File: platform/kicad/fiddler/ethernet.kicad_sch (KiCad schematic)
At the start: 33 parts, among them T1 PT61018PEL, U3 LAN8720A

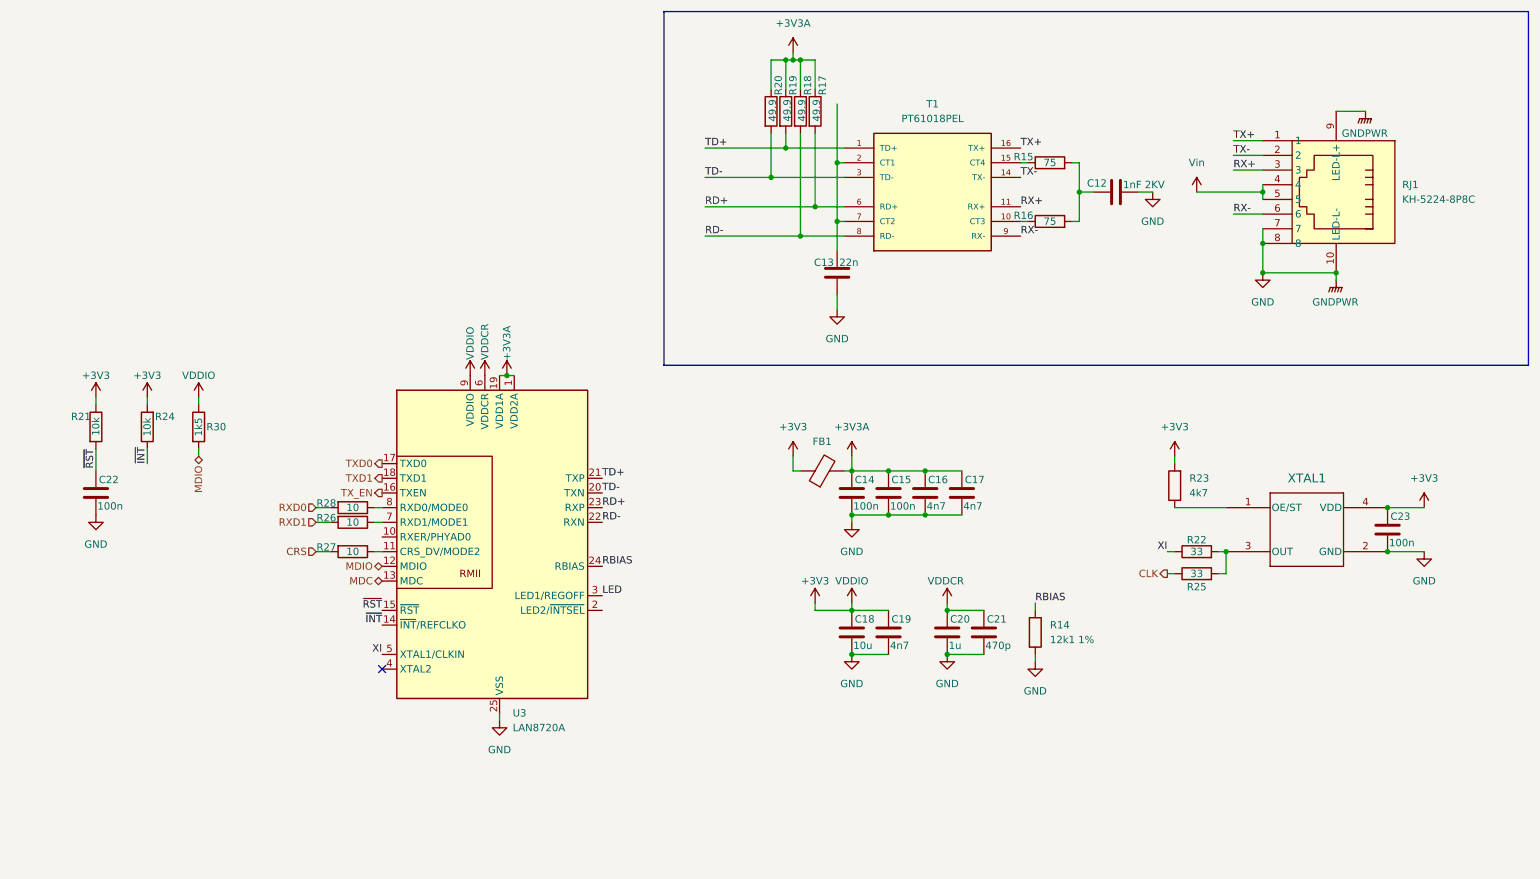
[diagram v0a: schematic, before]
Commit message: Fiddler Ray Speaker: Complete first revision
This change completes the first iteration schematic and layout for the fiddler ray speaker PCB.
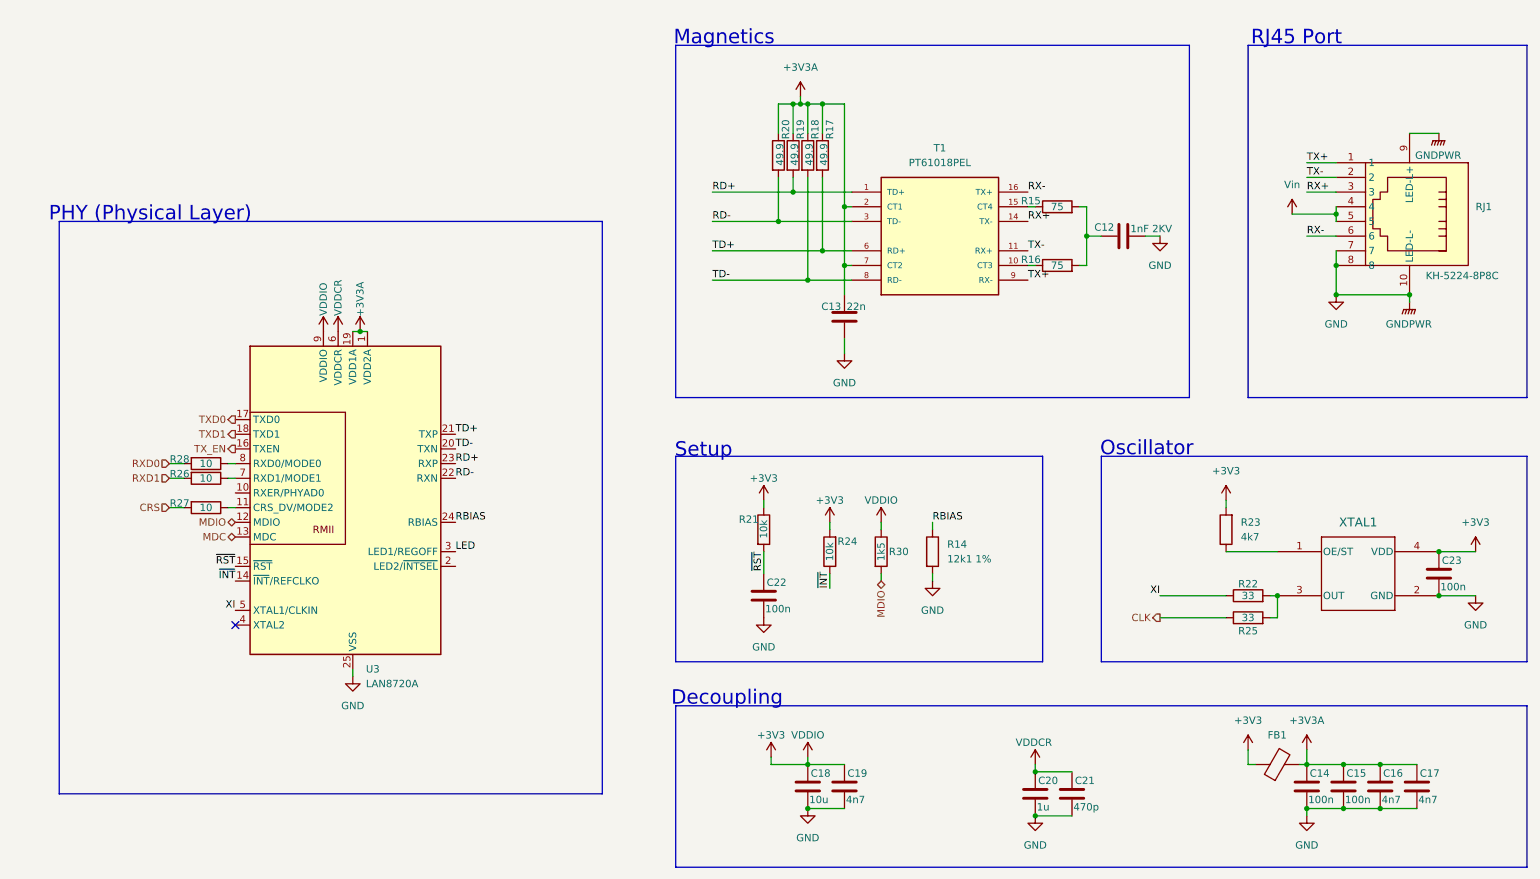
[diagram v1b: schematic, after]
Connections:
- net +3V3A: now also C13.2, T1.2 (CT1), T1.7 (CT2)
- net RD+: now also R19.2, T1.1 (TD+); no longer R17.2, T1.6 (RD+)
- net RD-: now also R20.2, T1.3 (TD-); no longer R18.2, T1.8 (RD-)
- net RX+: now also T1.14 (TX-); no longer T1.11 (RX+)
- net RX-: now also T1.16 (TX+); no longer T1.9 (RX-)
- net TD+: now also R17.2, T1.6 (RD+); no longer R19.2, T1.1 (TD+)
- net TD-: now also R18.2, T1.8 (RD-); no longer R20.2, T1.3 (TD-)
- net TX+: now also T1.9 (RX-); no longer T1.16 (TX+)
- net TX-: now also T1.11 (RX+); no longer T1.14 (TX-)
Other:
- note added: "Decoupling"
- note added: "Magnetics"
- note added: "Oscillator"
- note added: "PHY (Physical Layer)"
- note added: "RJ45 Port"
- note added: "Setup"
- company: (none) -> The Australian Ocean Laboratory
- title: (none) -> Fiddler Ray Speaker Unit V1
- moved on the sheet: C12, C13, C14, C15, C16, C17, C18, C19, C20, C21, C22, C23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

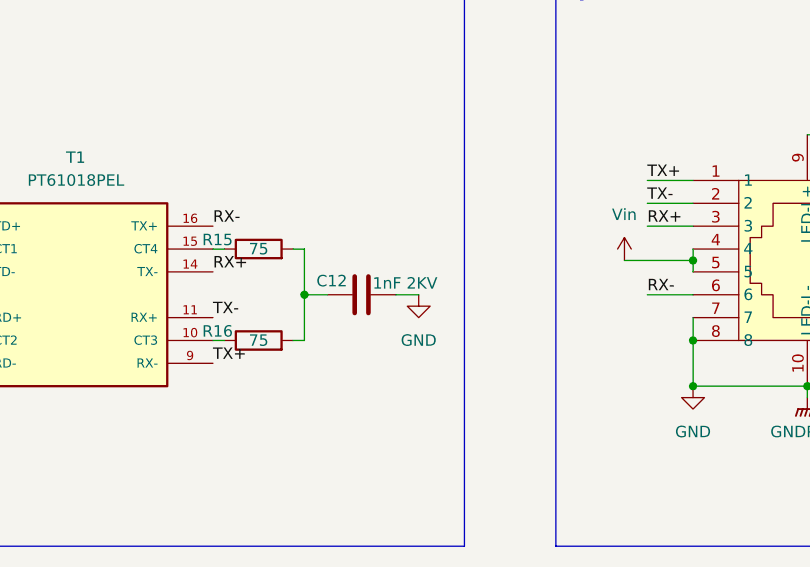
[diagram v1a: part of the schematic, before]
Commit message: Fiddler Ray Speaker: Production rev A
This change adds additional data to components to populate SPN for
the BOM via JLC
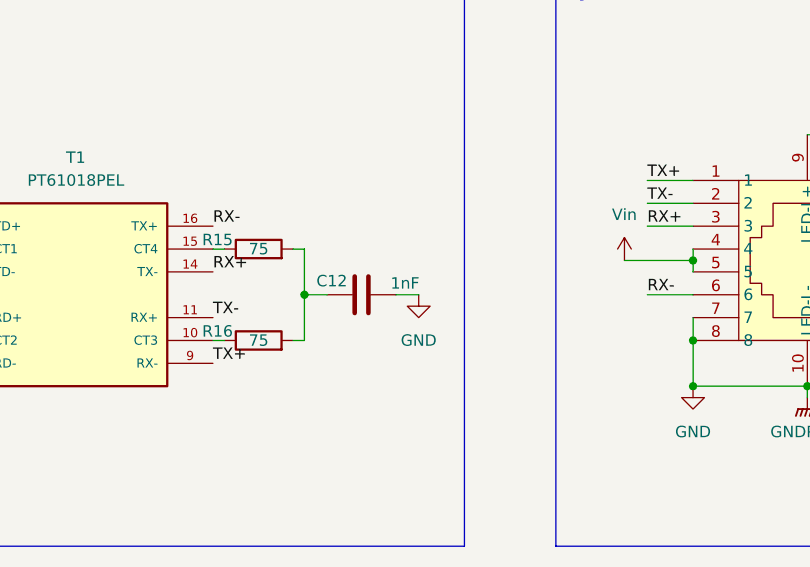
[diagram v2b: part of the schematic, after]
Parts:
- C12: value 1nF 2KV -> 1nF; footprint Capacitor_SMD:C_0603_1608Metric -> Capacitor_SMD:C_1206_3216Metric; LCSC Part # (none) -> C9196; Voltage Rating (none) -> 2kV
- C13: footprint Capacitor_SMD:C_0603_1608Metric -> Capacitor_SMD:C_2220_5750Metric; LCSC Part # (none) -> C784413; Voltage Rating (none) -> 2kV
- C14, C15, C22, C23: LCSC Part # (none) -> C14663
- C16, C17, C19: LCSC Part # (none) -> C53987
- C18: LCSC Part # (none) -> C19702
- C20: LCSC Part # (none) -> C15849
- C21: LCSC Part # (none) -> C1620
- FB1: LCSC Part # (none) -> C14709
- RJ1: LCSC Part C2683357 -> (none); LCSC Part # (none) -> C2683357
- T1: LCSC Part # (none) -> C840586
- U3: LCSC Part # (none) -> C45223
- XTAL1: LCSC Part # (none) -> C70716
